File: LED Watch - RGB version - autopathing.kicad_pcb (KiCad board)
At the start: 2 copper layers, 41.9 x 49.3 mm, 140 parts, among them J1 AVR-ISP-6, J2 Lipo, J3 Coin Cell, SW1 SW_DPST, SW2 SW_DPST, U10 B39D3RGB-F6C0001HOU1930, U100 B39D3RGB-F6C0001HOU1930, U101 B39D3RGB-F6C0001HOU1930, U102 B39D3RGB-F6C0001HOU1930, U103 B39D3RGB-F6C0001HOU1930, U104 B39D3RGB-F6C0001HOU1930, U105 B39D3RGB-F6C0001HOU1930, U106 B39D3RGB-F6C0001HOU1930, U107 B39D3RGB-F6C0001HOU1930, U108 B39D3RGB-F6C0001HOU1930, U109 B39D3RGB-F6C0001HOU1930, U11 B39D3RGB-F6C0001HOU1930, U110 B39D3RGB-F6C0001HOU1930, U111 B39D3RGB-F6C0001HOU1930, U112 B39D3RGB-F6C0001HOU1930, U113 B39D3RGB-F6C0001HOU1930, U114 B39D3RGB-F6C0001HOU1930, U115 B39D3RGB-F6C0001HOU1930, U116 B39D3RGB-F6C0001HOU1930, U117 B39D3RGB-F6C0001HOU1930, U118 B39D3RGB-F6C0001HOU1930, U119 B39D3RGB-F6C0001HOU1930, U12 B39D3RGB-F6C0001HOU1930, U120 B39D3RGB-F6C0001HOU1930, U121 B39D3RGB-F6C0001HOU1930, U122 B39D3RGB-F6C0001HOU1930, U123 B39D3RGB-F6C0001HOU1930, U124 B39D3RGB-F6C0001HOU1930, U125 B39D3RGB-F6C0001HOU1930, U126 B39D3RGB-F6C0001HOU1930, U127 B39D3RGB-F6C0001HOU1930, U128 B39D3RGB-F6C0001HOU1930, U129 B39D3RGB-F6C0001HOU1930, U13 B39D3RGB-F6C0001HOU1930, U130 B39D3RGB-F6C0001HOU1930, U131 B39D3RGB-F6C0001HOU1930, U132 B39D3RGB-F6C0001HOU1930, U133 B39D3RGB-F6C0001HOU1930, U134 BMI160, U135 ATmega165PA-M, U14 B39D3RGB-F6C0001HOU1930, U15 B39D3RGB-F6C0001HOU1930, U16 B39D3RGB-F6C0001HOU1930, U17 B39D3RGB-F6C0001HOU1930, U18 B39D3RGB-F6C0001HOU1930, U19 B39D3RGB-F6C0001HOU1930, U2 B39D3RGB-F6C0001HOU1930, U20 B39D3RGB-F6C0001HOU1930, U21 B39D3RGB-F6C0001HOU1930, U22 B39D3RGB-F6C0001HOU1930, U23 B39D3RGB-F6C0001HOU1930, U24 B39D3RGB-F6C0001HOU1930, U25 B39D3RGB-F6C0001HOU1930, U26 B39D3RGB-F6C0001HOU1930, U27 B39D3RGB-F6C0001HOU1930, U28 B39D3RGB-F6C0001HOU1930, U29 B39D3RGB-F6C0001HOU1930, U3 B39D3RGB-F6C0001HOU1930, U30 B39D3RGB-F6C0001HOU1930, U31 B39D3RGB-F6C0001HOU1930, U32 B39D3RGB-F6C0001HOU1930, U33 B39D3RGB-F6C0001HOU1930, U34 B39D3RGB-F6C0001HOU1930, U35 B39D3RGB-F6C0001HOU1930, U36 B39D3RGB-F6C0001HOU1930, U37 B39D3RGB-F6C0001HOU1930, U38 B39D3RGB-F6C0001HOU1930, U39 B39D3RGB-F6C0001HOU1930, U4 B39D3RGB-F6C0001HOU1930, U40 B39D3RGB-F6C0001HOU1930, U41 B39D3RGB-F6C0001HOU1930, U42 B39D3RGB-F6C0001HOU1930, U43 B39D3RGB-F6C0001HOU1930, U44 B39D3RGB-F6C0001HOU1930, U45 B39D3RGB-F6C0001HOU1930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

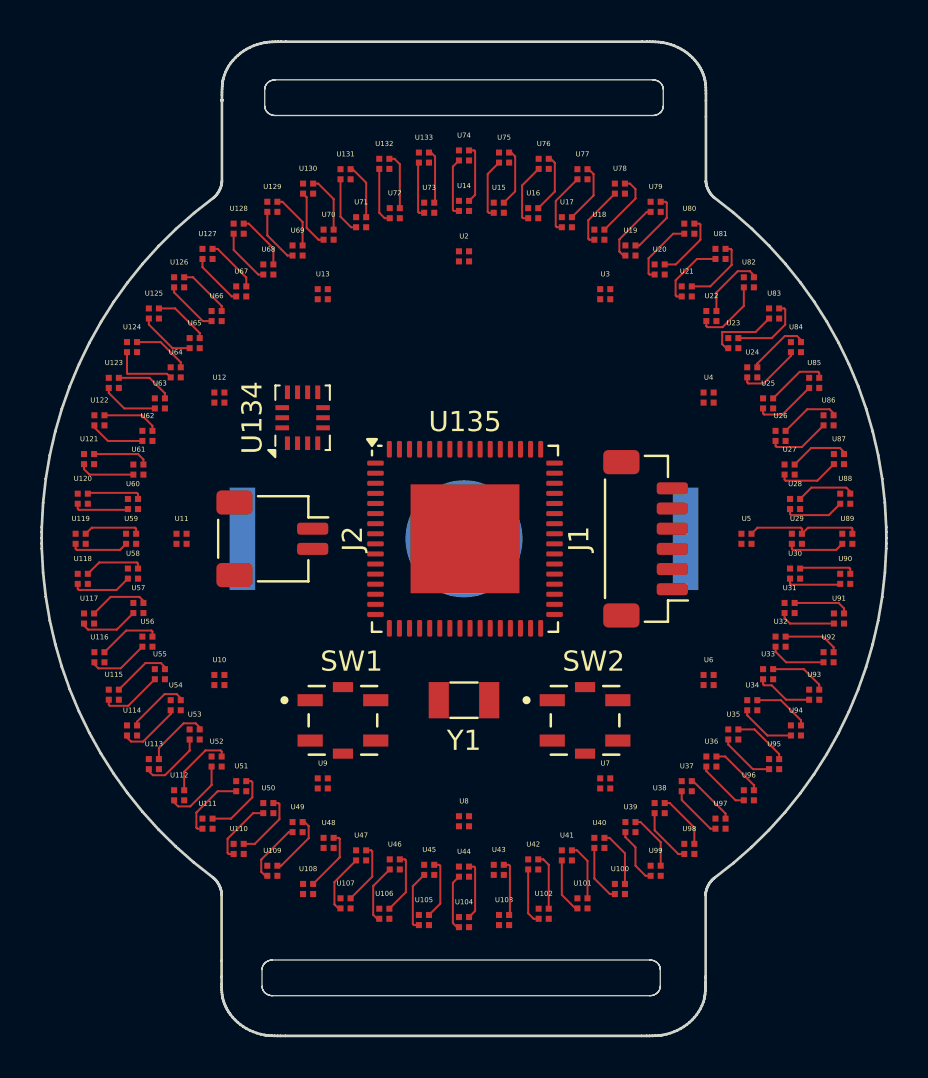
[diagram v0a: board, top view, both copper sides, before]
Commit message: adjusted clocking and spacings.. ready for routing again
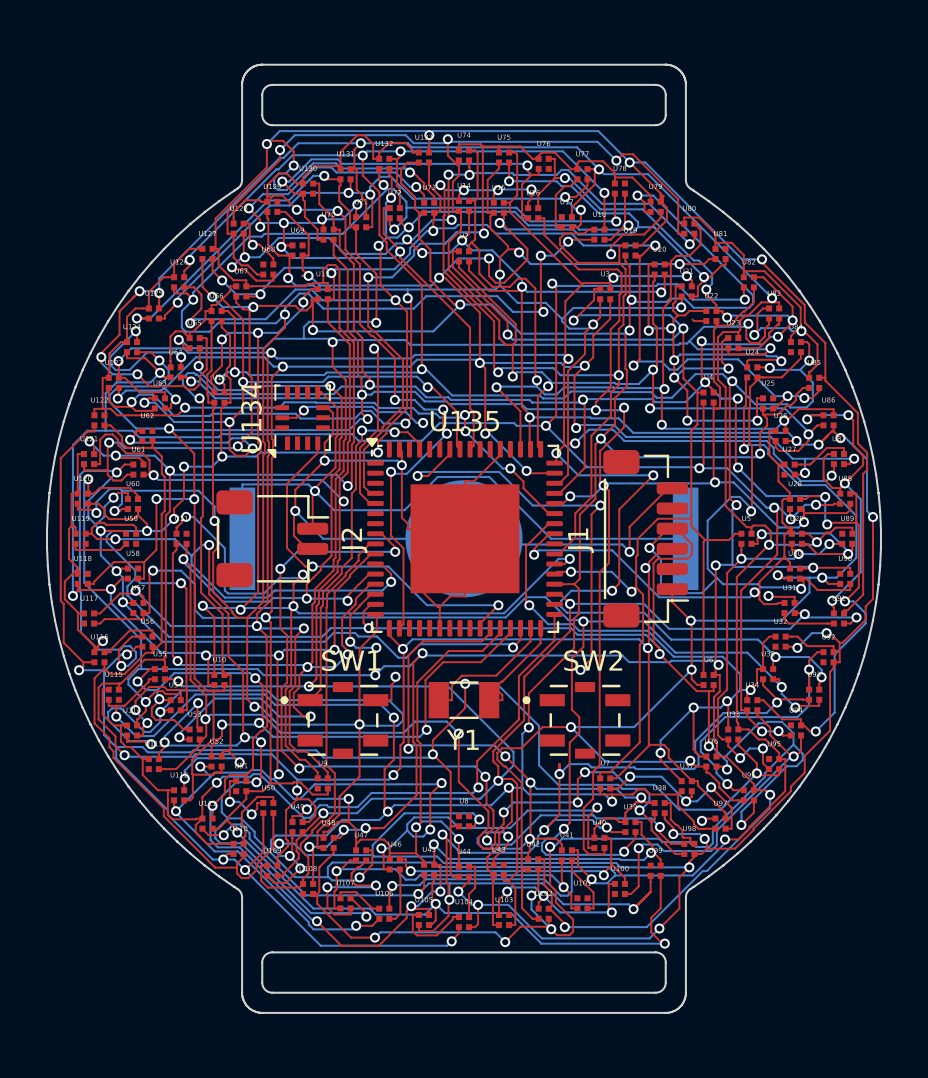
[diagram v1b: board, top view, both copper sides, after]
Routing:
- net /G2: track 0.00 -> 231.8 mm, vias 0 -> 26
- net /G5: track 0.00 -> 224.4 mm, vias 0 -> 27
- net /G1: track 0.00 -> 200.0 mm, vias 0 -> 26
- net /B5: track 25.9 -> 212.7 mm, vias 0 -> 22
- net /R5: track 29.1 -> 208.4 mm, vias 0 -> 25
- net /G6: track 0.00 -> 174.2 mm, vias 0 -> 21
- net /G3: track 0.00 -> 172.7 mm, vias 0 -> 15
- net /R4: track 32.9 -> 198.3 mm, vias 0 -> 21
- net /R6: track 28.8 -> 192.2 mm, vias 0 -> 17
- net /B3: track 30.7 -> 193.7 mm, vias 0 -> 25
- net /B6: track 26.2 -> 184.3 mm, vias 0 -> 19
- net /B1: track 29.7 -> 176.1 mm, vias 0 -> 16
- net /B2: track 30.3 -> 170.1 mm, vias 0 -> 20
- net /G4: track 0.00 -> 139.2 mm, vias 0 -> 20
- net /R3: track 30.2 -> 168.8 mm, vias 0 -> 23
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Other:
- board size 41.9 x 49.3 mm -> 41.3 x 47 mm
